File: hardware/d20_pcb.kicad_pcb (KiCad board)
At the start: 2 copper layers, 45.1 x 57.8 mm, 38 parts, among them J1 Conn_01x06_Socket, J2 Conn_01x01_Pin, SW1 SW_SPST, SW2 SW_Push, U1 ATtiny84-20P

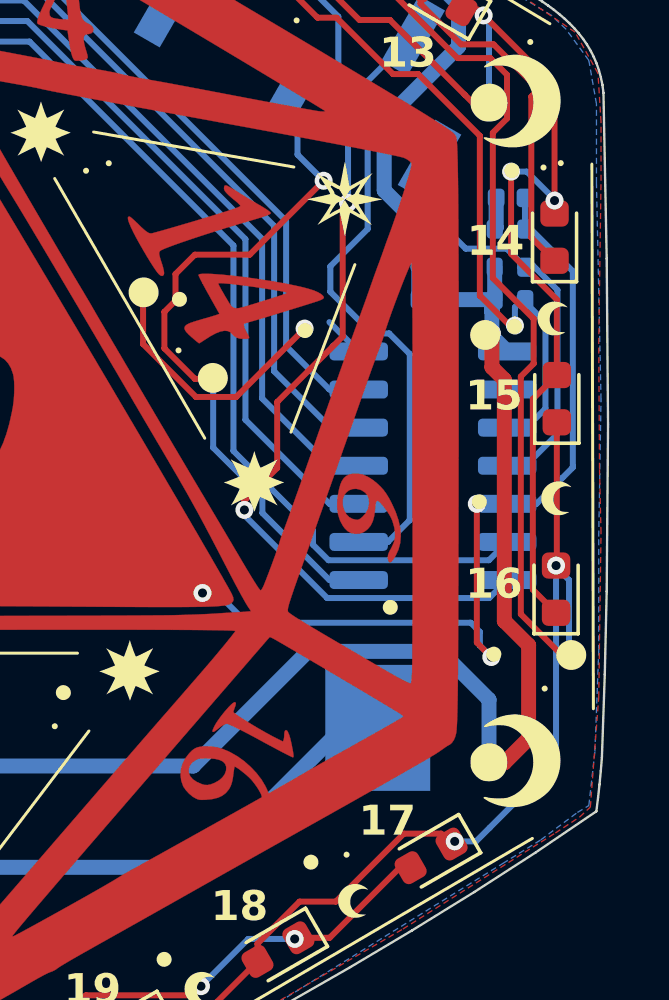
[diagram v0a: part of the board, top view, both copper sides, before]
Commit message: HW: Add d20v3
Changes:
- move touchpad to analog pin
- resize map artwork
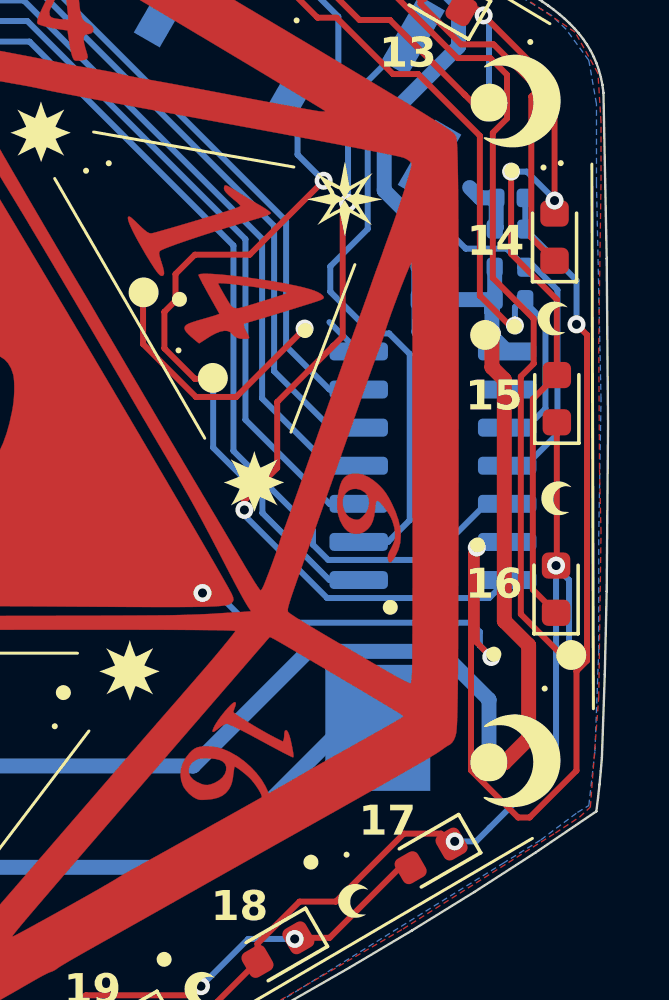
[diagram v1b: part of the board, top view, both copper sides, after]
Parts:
- added REF**: d20_caldereth, d20_pcb:d20_caldereth, F.Cu at (133.7, 102.0)
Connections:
- U1 pad 5: PAD -> E
- U1 pad 6: E -> PAD
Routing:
- net PAD: track 37.5 -> 56.5 mm, vias 3 -> 4
- net GND: track 12.4 -> 15.4 mm
